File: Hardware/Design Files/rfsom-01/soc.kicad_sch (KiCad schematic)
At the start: 0 parts

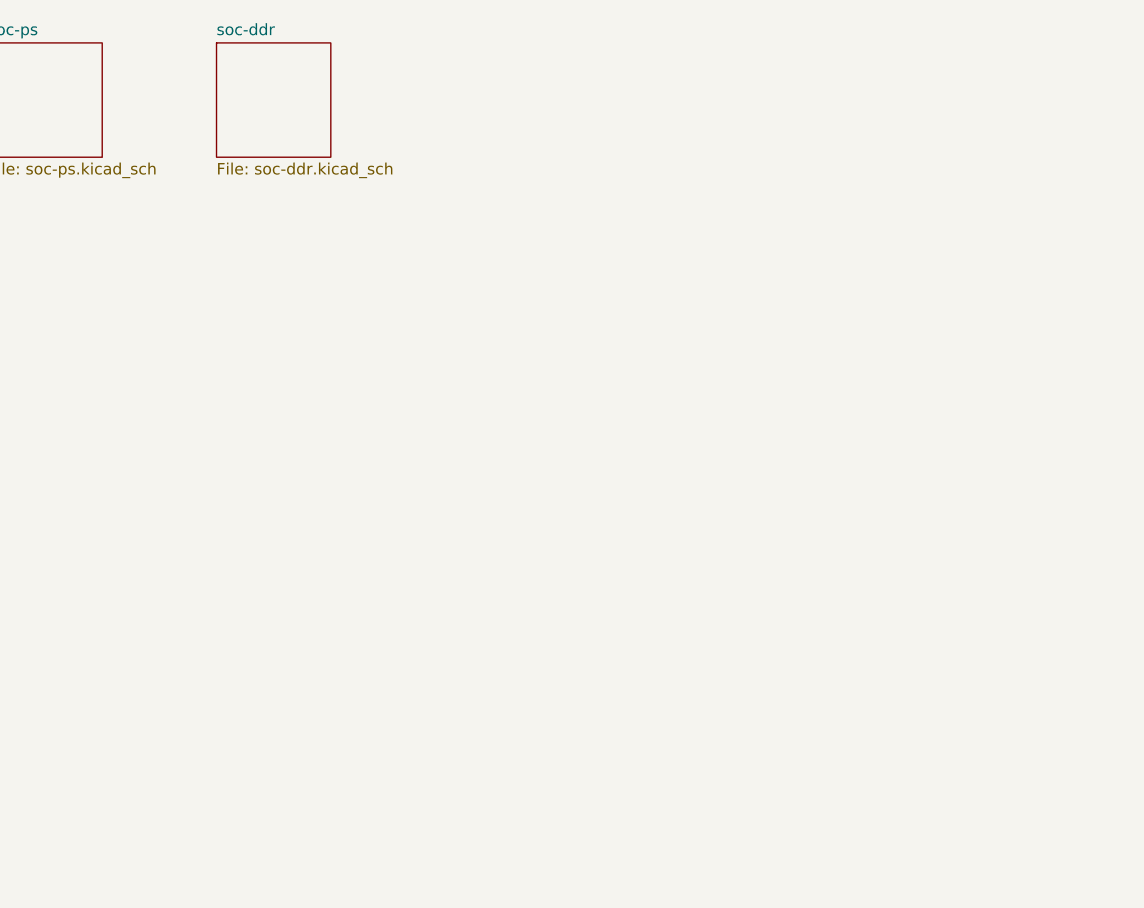
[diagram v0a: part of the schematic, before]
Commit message: ddr progress; added more conns;
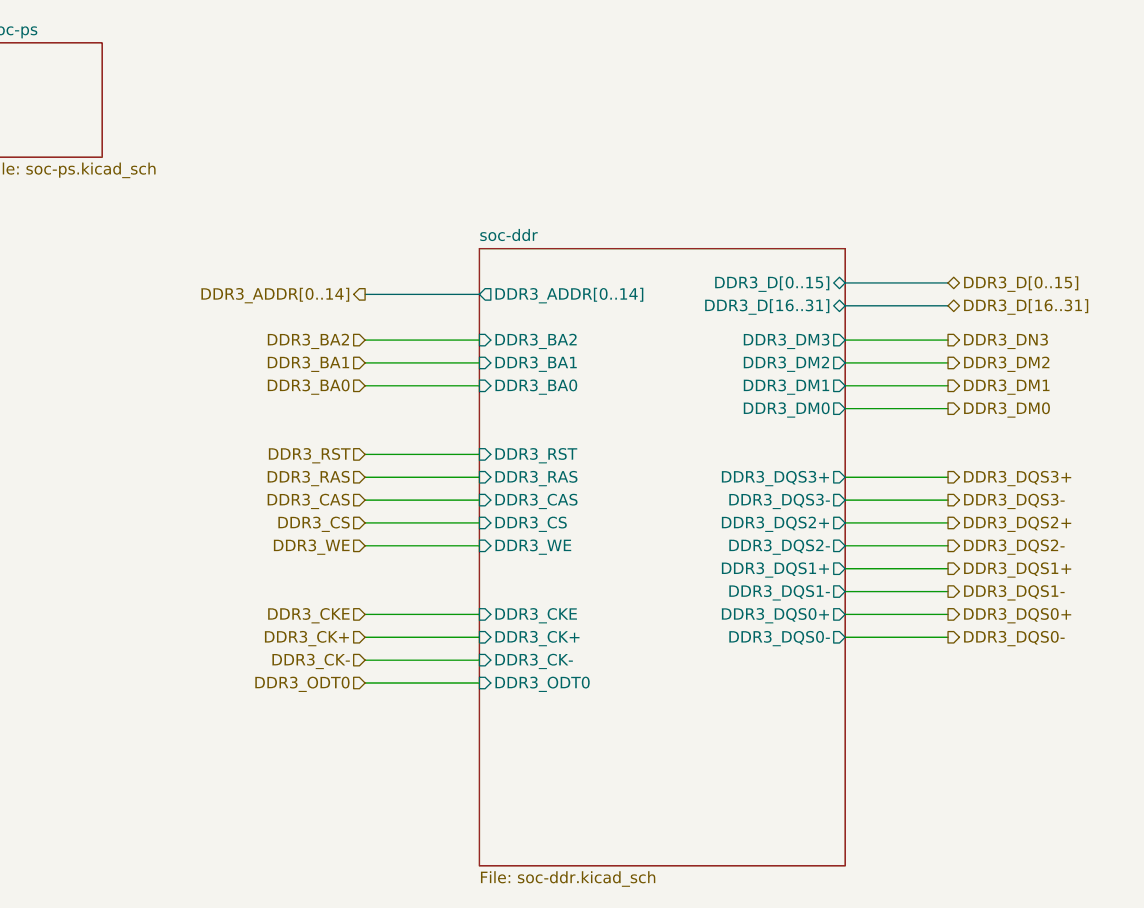
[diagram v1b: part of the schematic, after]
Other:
- sheet soc-ddr ports: added DDR3_ADDR[0..14], DDR3_BA0, DDR3_BA1, DDR3_BA2, DDR3_CAS, DDR3_CK+, DDR3_CK-, DDR3_CKE, DDR3_CS, DDR3_DM0, DDR3_DM1, DDR3_DM2, DDR3_DM3, DDR3_DQS0+, DDR3_DQS0-, DDR3_DQS1+, DDR3_DQS1-, DDR3_DQS2+, DDR3_DQS2-, DDR3_DQS3+, DDR3_DQS3-, DDR3_D[0..15], DDR3_D[16..31], DDR3_ODT0, DDR3_RAS, DDR3_RST, DDR3_WE; removed none

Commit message: ps progress; added ftdi; mezz pinout pedinging;
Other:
- sheet soc-ddr ports: added none; removed DDR3_ADDR[0..14], DDR3_BA0, DDR3_BA1, DDR3_BA2, DDR3_CAS, DDR3_CK+, DDR3_CK-, DDR3_CKE, DDR3_CS, DDR3_DM0, DDR3_DM1, DDR3_DM2, DDR3_DM3, DDR3_DQS0+, DDR3_DQS0-, DDR3_DQS1+, DDR3_DQS1-, DDR3_DQS2+, DDR3_DQS2-, DDR3_DQS3+, DDR3_DQS3-, DDR3_D[0..15], DDR3_D[16..31], DDR3_ODT0, DDR3_RAS, DDR3_RST, DDR3_WE

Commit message: some ddr routing progress; layerstack per pcbway standard options, review reqd; commit prior to ddr split;
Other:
- sheet soc-ps ports: added ENET0_MDC, ENET0_MDIO, ENET0_RXCLK, ENET0_RXCTL_R, ENET0_RXD0_R, ENET0_RXD1_R, ENET0_RXD2_R, ENET0_RXD3_R, ENET0_SYSCLK, ENET0_TXCLK_R, ENET0_TXCTL_R, ENET0_TXD0_R, ENET0_TXD1_R, ENET0_TXD2_R, ENET0_TXD3_R, EXT_SD_CD, EXT_SD_CLK, EXT_SD_CMD, EXT_SD_D0, EXT_SD_D1, EXT_SD_D2, EXT_SD_D3, EXT_VADC+, EXT_VADC-, JTAG_TCK_R, JTAG_TDI_R, JTAG_TDO_R, JTAG_TMS_R, USBH_OE, ~{ETH_RST}; removed none

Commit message: added starage, usb sch; more design progress in sch;
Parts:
- added C105, C109: CL05B104KA5NNNC, Capacitor_SMD:C_0402_1005Metric, symbol Capacitors:CL05B104KA5NNNC
- added J6, J7, J8: ~, Jumper:SolderJumper-2_P1.3mm_Open_RoundedPad1.0x1.5mm, symbol Miscellaneous:JMP_SLD
- added R44: RC0603FR-0747K5L, Resistor_SMD:R_0603_1608Metric, symbol Resistors:RC0603FR-0747K5L
- added U7: TXS02612RTWR, ICs:QFN-24-1EP_4x4mm_P0.5mm, symbol ICs:TXS02612RTWR
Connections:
- net EXT_SD_CD: now also J8.1
- net EXT_SD_CLK: now also U7.13 (CLK_B1)
- net EXT_SD_CMD: now also U7.12 (CMD_B1)
- net EXT_SD_D0: now also U7.14 (DAT0_B1)
- net EXT_SD_D1: now also U7.15 (DAT1_B1)
- net EXT_SD_D2: now also U7.8 (DAT2_B1)
- net EXT_SD_D3: now also U7.10 (DAT3_B1)
- new net +VCC_1V8: C105.1, J6.2, U7.5 (VCCA)
- new net +VCC_3V3: C109.1, U7.17 (VCC_B1), U7.21 (VCC_B0)
- new net GND: C105.2, C109.2, R44.2, U7.11 (GND), U7.2 (GND), U7.25 (EP)
- new net SDC_CD: J7.2
- new net SDC_CLK: U7.19 (CLK_B0)
- new net SDC_CMD: U7.20 (CMD_B0)
- new net SDC_DAT0: U7.18 (DAT0_B0)
- new net SDC_DAT1: U7.16 (DAT1_B0)
- new net SDC_DAT2: U7.23 (DAT2_B0)
- new net SDC_DAT3: U7.22 (DAT3_B0)
- new net SD_CLK: U7.9 (CLKA)
- new net SD_CMD: U7.4 (CMDA)
- new net SD_D0: U7.6 (DAT0A)
- new net SD_D1: U7.7 (DAT1A)
- new net SD_D2: U7.1 (DAT2A)
- new net SD_D3: U7.3 (DAT3A)
- new net SD_SEL: J6.1, R44.1, U7.24 (SEL)
- new net soc-ps/SD0_CD: J7.1, J8.2
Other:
- sheet soc-ddr renamed soc-ram
- added sheet storage (storage.kicad_sch)
- added sheet usb (usb.kicad_sch)
- sheet soc-ps ports: added QSPI_CLK/MIO6, QSPI_DQ0/MIO2, QSPI_DQ1/MIO3, QSPI_DQ2/MIO4, QSPI_DQ3/MIO5, SD0_CD, SD0_CLK, SD0_CMD, SD0_D0, SD0_D1, SD0_D2, SD0_D3, SD1_CLK, SD1_CMD, SD1_D0, SD1_D1, SD1_D2, SD1_D3, USB0_CLK, USB0_DATA0, USB0_DATA1, USB0_DATA2, USB0_DATA3, USB0_DATA4, USB0_DATA5, USB0_DATA6, USB0_DATA7, USB0_DIR, USB0_NXT, USB0_STP, ZYNQ_UART0_RXD, ZYNQ_UART0_TXD, ~{QSPI_CS}, ~{USB_RST}; removed EXT_SD_CD, EXT_SD_CLK, EXT_SD_CMD, EXT_SD_D0, EXT_SD_D1, EXT_SD_D2, EXT_SD_D3, USBH_OE

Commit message: routing changes; added mezzanine; added pl ram;
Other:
- moved on the sheet: C105, C109, J6, R44, U7
